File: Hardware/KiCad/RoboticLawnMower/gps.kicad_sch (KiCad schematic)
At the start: 1 part, among them J13 I2C 0

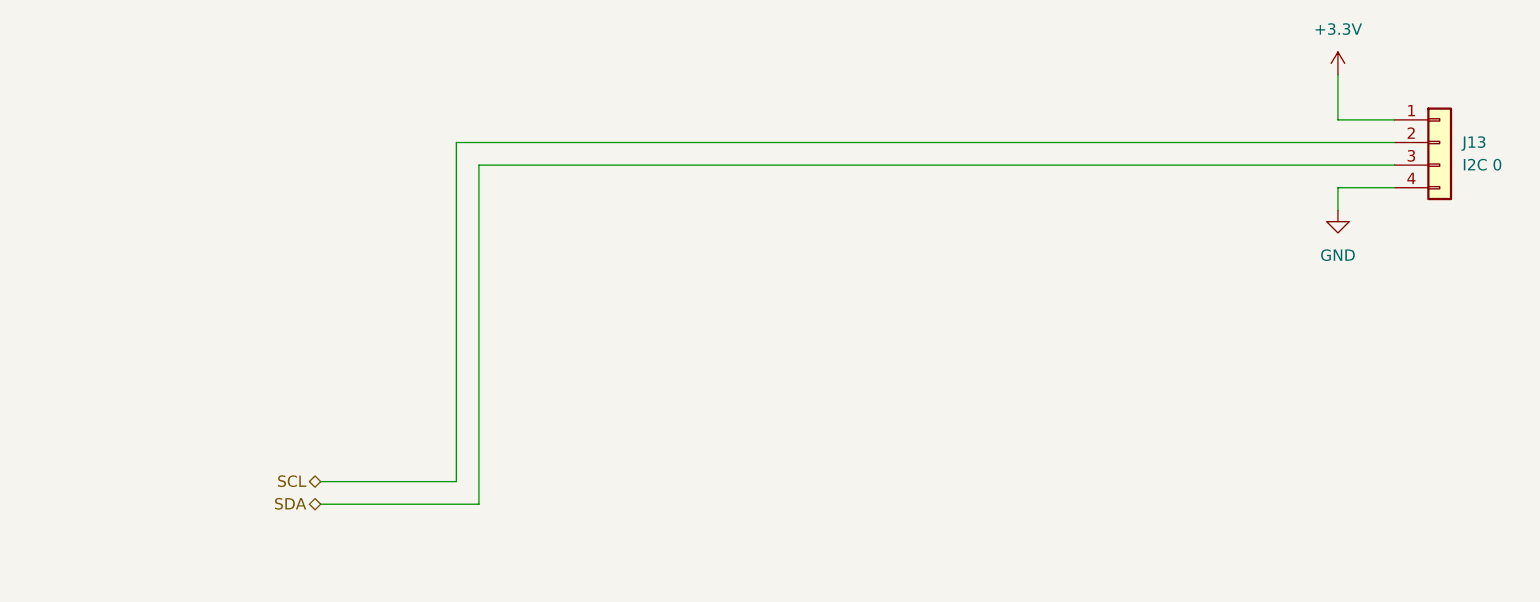
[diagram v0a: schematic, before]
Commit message: Schaltplan & Layout Änderung
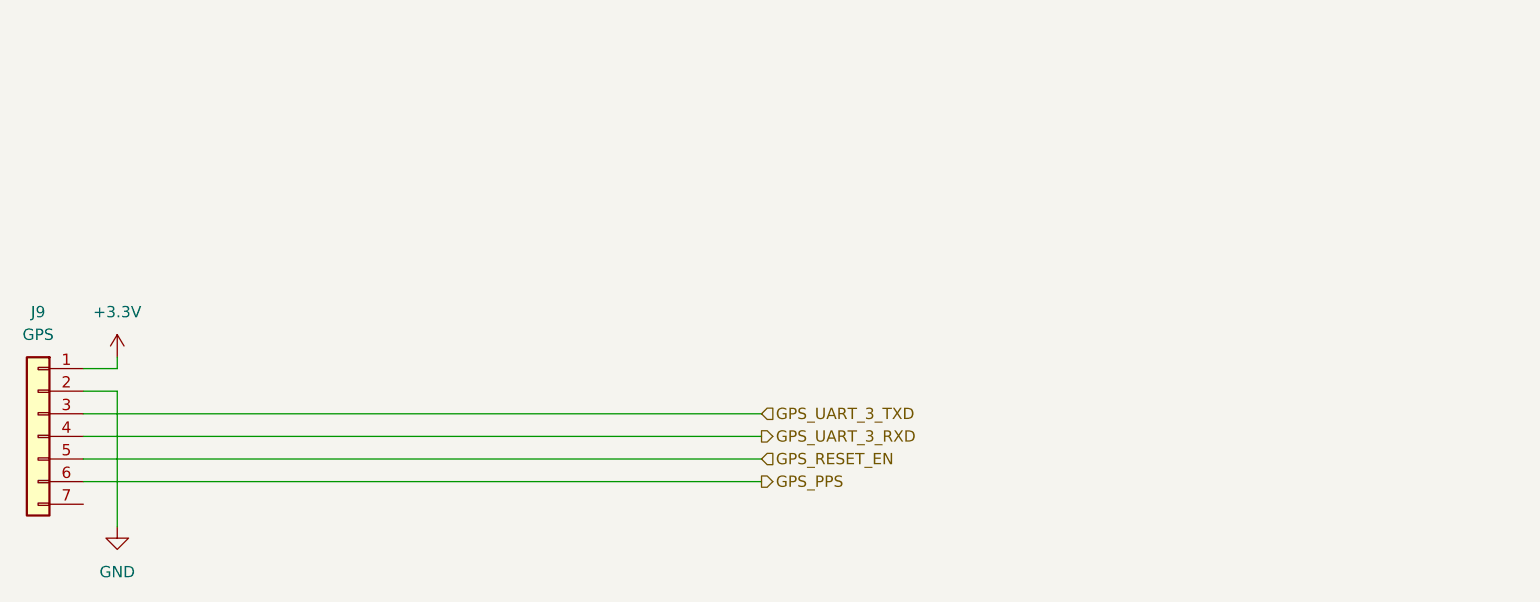
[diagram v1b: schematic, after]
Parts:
- removed J13: I2C 0, Connector_JST:JST_XA_B04B-XASK-1_1x04_P2.50mm_Vertical, symbol Connector_Generic:Conn_01x04
- added J9: GPS, Connector_JST:JST_XA_B07B-XASK-1_1x07_P2.50mm_Vertical, symbol Connector_Generic:Conn_01x07
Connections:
- net +3.3V: now also J9.1 (Pin_1)
- net GND: now also J9.2 (Pin_2)
- new net GPS_PPS: J9.6 (Pin_6)
- new net GPS_RESET_EN: J9.5 (Pin_5)
- new net GPS_UART_3_RXD: J9.4 (Pin_4)
- new net GPS_UART_3_TXD: J9.3 (Pin_3)
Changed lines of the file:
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@@
 (kicad_sch (version 20211123) (generator eeschema)
   (paper "A4")
-  (wire (pts (xy 209.55 34.29) (xy 106.68 34.29))
+  (wire (pts (xy 62.23 57.15) (xy 66.04 57.15))
     (stroke (width 0) (type default) (color 0 0 0 0))
   )
-  (wire (pts (xy 203.2 29.21) (xy 209.55 29.21))
+  (wire (pts (xy 62.23 67.31) (xy 138.43 67.31))
     (stroke (width 0) (type default) (color 0 0 0 0))
   )
-  (wire (pts (xy 106.68 34.29) (xy 106.68 72.39))
+  (wire (pts (xy 66.04 57.15) (xy 66.04 55.88))
     (stroke (width 0) (type default) (color 0 0 0 0))
   )
-  (wire (pts (xy 203.2 36.83) (xy 203.2 39.37))
+  (wire (pts (xy 62.23 62.23) (xy 138.43 62.23))
     (stroke (width 0) (type default) (color 0 0 0 0))
   )
-  (wire (pts (xy 88.9 72.39) (xy 106.68 72.39))
+  (wire (pts (xy 62.23 64.77) (xy 138.43 64.77))
     (stroke (width 0) (type default) (color 0 0 0 0))
   )
-  (wire (pts (xy 203.2 24.13) (xy 203.2 29.21))
+  (wire (pts (xy 62.23 59.69) (xy 66.04 59.69))
     (stroke (width 0) (type default) (color 0 0 0 0))
   )
-  (wire (pts (xy 88.9 69.85) (xy 104.14 69.85))
+  (wire (pts (xy 62.23 69.85) (xy 138.43 69.85))
     (stroke (width 0) (type default) (color 0 0 0 0))
   )
-  (wire (pts (xy 209.55 31.75) (xy 104.14 31.75))
+  (wire (pts (xy 66.04 59.69) (xy 66.04 74.93))
     (stroke (width 0) (type default) (color 0 0 0 0))
   )
-  (wire (pts (xy 104.14 31.75) (xy 104.14 69.85))
-    (stroke (width 0) (type default) (color 0 0 0 0))
+  (hierarchical_label "GPS_PPS" (shape output) (at 138.43 69.85 0)
+    (effects (font (size 1.27 1.27)) (justify left))
   )
-  (wire (pts (xy 203.2 36.83) (xy 209.55 36.83))
-    (stroke (width 0) (type default) (color 0 0 0 0))
+  (hierarchical_label "GPS_UART_3_TXD" (shape input) (at 138.43 62.23 0)
+    (effects (font (size 1.27 1.27)) (justify left))
   )
-  (hierarchical_label "SCL" (shape bidirectional) (at 88.9 69.85 180)
-    (effects (font (size 1.27 1.27)) (justify right))
+  (hierarchical_label "GPS_UART_3_RXD" (shape output) (at 138.43 64.77 0)
+    (effects (font (size 1.27 1.27)) (justify left))
   )
-  (hierarchical_label "SDA" (shape bidirectional) (at 88.9 72.39 180)
-    (effects (font (size 1.27 1.27)) (justify right))
+  (hierarchical_label "GPS_RESET_EN" (shape input) (at 138.43 67.31 0)
+    (effects (font (size 1.27 1.27)) (justify left))
   )
-  (symbol (lib_id "power:GND") (at 203.2 39.37 0) (unit 1)
+  (symbol (lib_id "power:+3.3V") (at 66.04 55.88 0) (mirror y) (unit 1)
     (in_bom yes) (on_board yes) (fields_autoplaced)
-    (property "Reference" "#PWR069" (id 0) (at 203.2 45.72 0)
+    (property "Reference" "#PWR033" (id 0) (at 66.04 59.69 0)
       (effects (font (size 1.27 1.27)) hide)
     )
-    (property "Value" "GND" (id 1) (at 203.2 44.45 0))
-    (property "Footprint" "" (id 2) (at 203.2 39.37 0)
+    (property "Value" "+3.3V" (id 1) (at 66.04 50.8 0))
+    (property "Footprint" "" (id 2) (at 66.04 55.88 0)
       (effects (font (size 1.27 1.27)) hide)
     )
-    (property "Datasheet" "" (id 3) (at 203.2 39.37 0)
+    (property "Datasheet" "" (id 3) (at 66.04 55.88 0)
       (effects (font (size 1.27 1.27)) hide)
     )
     (pin "1")
   )
-  (symbol (lib_id "power:+3.3V") (at 203.2 24.13 0) (unit 1)
+  (symbol (lib_id "power:GND") (at 66.04 74.93 0) (mirror y) (unit 1)
     (in_bom yes) (on_board yes) (fields_autoplaced)
-    (property "Reference" "#PWR039" (id 0) (at 203.2 27.94 0)
+    (property "Reference" "#PWR034" (id 0) (at 66.04 81.28 0)
       (effects (font (size 1.27 1.27)) hide)
     )
-    (property "Value" "+3.3V" (id 1) (at 203.2 19.05 0))
-    (property "Footprint" "" (id 2) (at 203.2 24.13 0)
+    (property "Value" "GND" (id 1) (at 66.04 80.01 0))
+    (property "Footprint" "" (id 2) (at 66.04 74.93 0)
       (effects (font (size 1.27 1.27)) hide)
     )
-    (property "Datasheet" "" (id 3) (at 203.2 24.13 0)
+    (property "Datasheet" "" (id 3) (at 66.04 74.93 0)
       (effects (font (size 1.27 1.27)) hide)
     )
     (pin "1")
   )
-  (symbol (lib_id "Connector_Generic:Conn_01x04") (at 214.63 31.75 0) (unit 1)
+  (symbol (lib_id "Connector_Generic:Conn_01x07") (at 57.15 64.77 0) (mirror y) (unit 1)
     (in_bom yes) (on_board yes) (fields_autoplaced)
-    (property "Reference" "J13" (id 0) (at 217.17 31.7499 0)
-      (effects (font (size 1.27 1.27)) (justify left))
-    )
-    (property "Value" "I2C 0" (id 1) (at 217.17 34.2899 0)
-      (effects (font (size 1.27 1.27)) (justify left))
-    )
-    (property "Footprint" "Connector_JST:JST_XA_B04B-XASK-1_1x04_P2.50mm_Vertical" (id 2) (at 214.63 31.75 0)
+    (property "Reference" "J9" (id 0) (at 57.15 50.8 0))
+    (property "Value" "GPS" (id 1) (at 57.15 53.34 0))
+    (property "Footprint" "Connector_JST:JST_XA_B07B-XASK-1_1x07_P2.50mm_Vertical" (id 2) (at 57.15 64.77 0)
       (effects (font (size 1.27 1.27)) hide)
     )
-    (property "Datasheet" "~" (id 3) (at 214.63 31.75 0)
+    (property "Datasheet" "~" (id 3) (at 57.15 64.77 0)
       (effects (font (size 1.27 1.27)) hide)
     )
@@
     (pin "3")
     (pin "4")
+    (pin "5")
+    (pin "6")
+    (pin "7")
   )
 )

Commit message: Layout ready add gerber file
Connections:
- net GPS_MOD_EN: now reaches J9.7 (Pin_7)
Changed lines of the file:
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@@
+    (stroke (width 0) (type default) (color 0 0 0 0))
+  )
+  (wire (pts (xy 62.23 72.39) (xy 138.43 72.39))
     (stroke (width 0) (type default) (color 0 0 0 0))
   )
@@
     (effects (font (size 1.27 1.27)) (justify left))
   )
+  (hierarchical_label "GPS_MOD_EN" (shape input) (at 138.43 72.39 0)
+    (effects (font (size 1.27 1.27)) (justify left))
+  )
